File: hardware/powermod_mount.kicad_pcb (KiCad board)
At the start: 4 copper layers, 76 x 46 mm, 76 parts, among them J1 USB_C_IN, J2 USB_C_OUT, J3 JST_PH_2, J4 STEMMA_QT, J5 UPDI_HDR, Q1 AON7407, Q2 AON7407, Q3 BSS138, SW1 BUTTON, U1 BM8563, U2 ATtiny1617, U3 TPS63020DSJR, U4 TP4056, U5 XC6206P332MR, Y1 32.768kHz

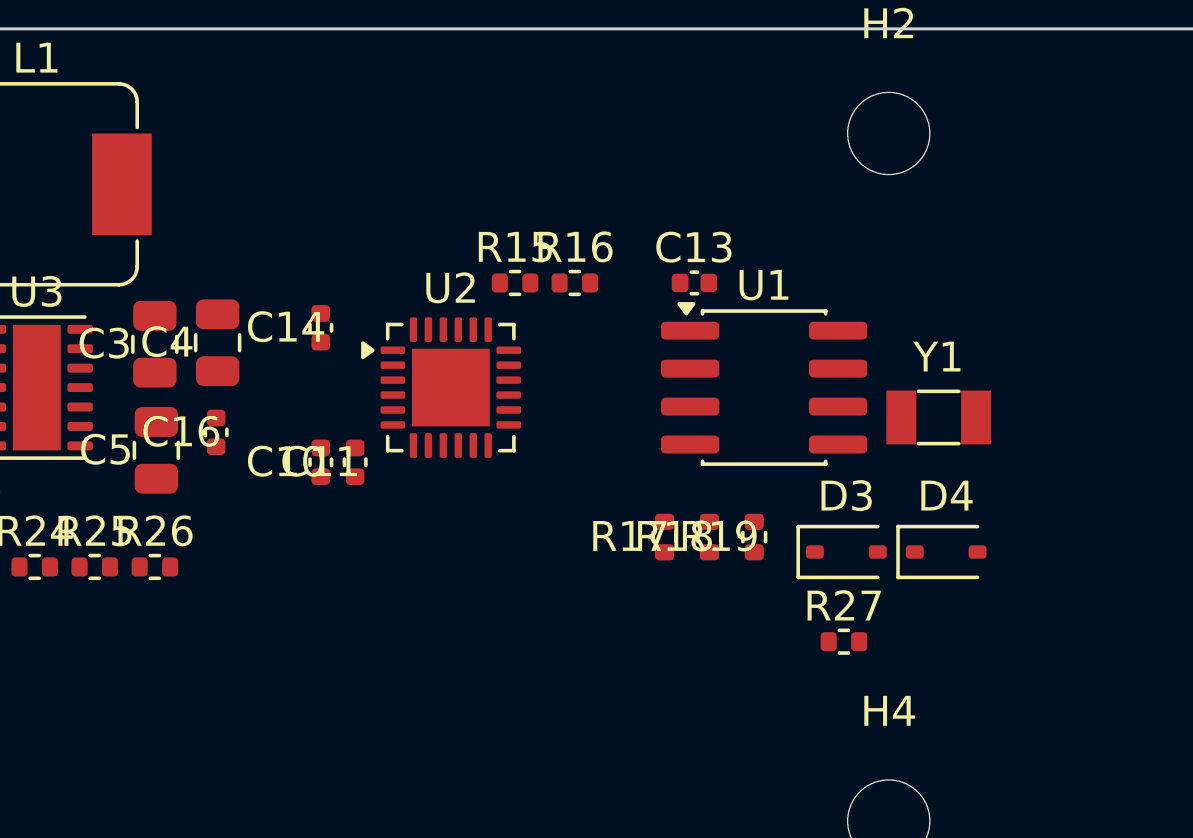
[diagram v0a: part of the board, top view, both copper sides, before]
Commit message: attiny: swap MCU to ATtiny1616 SOIC-20 — breaks the QFN routing wall
The 24-pin QFN (0.5mm pitch) was the persistent autorouting blocker: two of
its pins could never escape, boxed in by their routed neighbours, and no
placement or router technique moved them. Swapping to the ATtiny1616 in
SOIC-20 (1.27mm pitch, 2.5x coarser, no exposed pad, hand-solderable) removes
that wall entirely -- verified: the MCU pins (3V3, Q1_GATE_DRV) that were stuck
across every prior attempt now route, and the residual is ordinary nets
(VBUS/VOUT pour connections, GND stitching), no escape wall.

Electrical: we used exactly 18 signals and the SOIC-20 has exactly 18 I/O, so
it fits -- at the cost of the 4 spare pins the 24-pin had. Four signals moved
off pins the 20-pin package lacks (LED_BAT_A/B off PB6/PB7 -> PA6/PA7, CHG_CE
off PC4 -> PC0, RTC_SCL off PC5 -> PC1); all are plain GPIO and the async-wake
(PC2/PA2), TWI (PB0/PB1), ADC (PA4/PA5) and UPDI (PA0) pins are unchanged.

Pinout taken from KiCad's ATtiny406-S base symbol (the shared 20-pin tinyAVR-1
map), NOT a web summary (which had it wrong). Footprint SOIC-20W_7.5x12.8mm.
LCSC C2891852 to confirm at order time. netlist self-test + ERC both clean
(72 components, 231 pins). On the attiny-soic20 branch.

Co-Authored-By: Claude Opus 4.8 <noreply@anthropic.com>
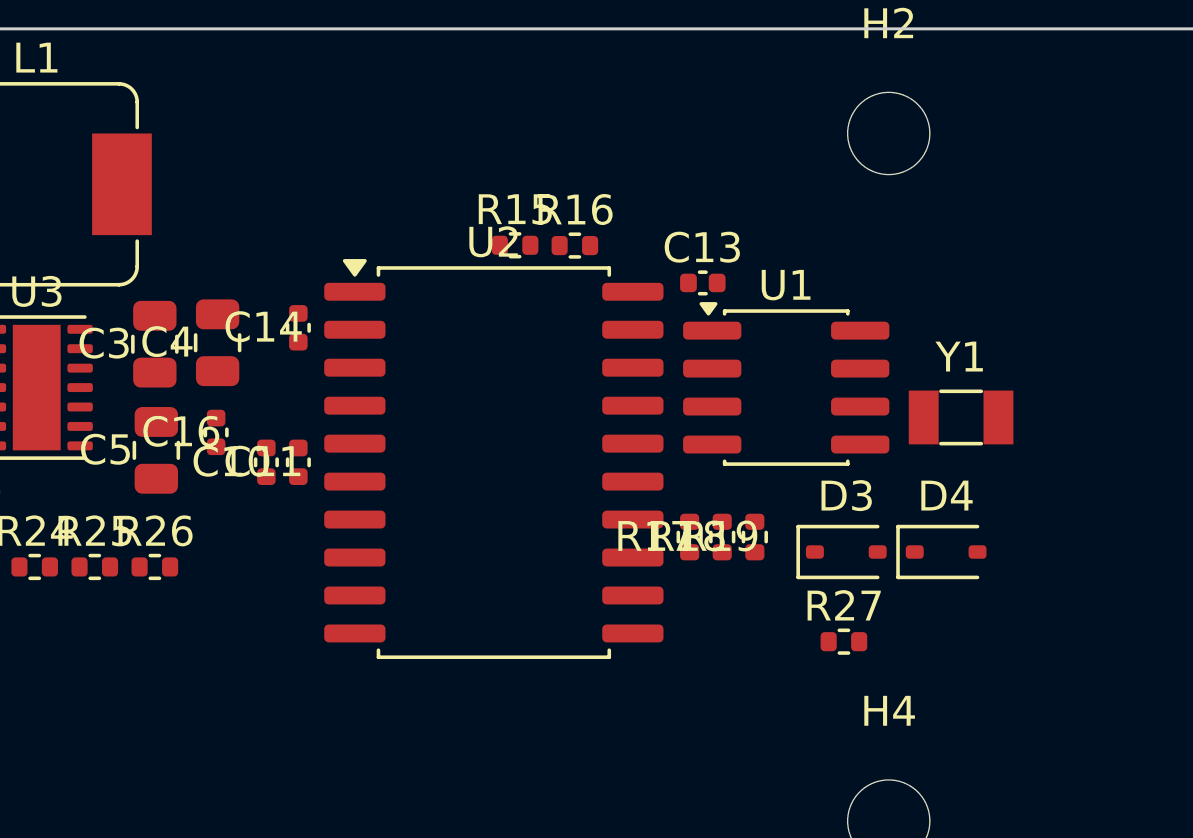
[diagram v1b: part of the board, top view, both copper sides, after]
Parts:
- U2: value ATtiny1617 -> ATtiny1616; footprint QFN-24-1EP_4x4mm_P0.5mm_EP2.6x2.6mm -> SOIC-20W_7.5x12.8mm_P1.27mm
- moved U2 2.89 mm to (48.3, 14.5)
- moved C11 1.90 mm to (41.8, 14.5)
- moved C10 1.82 mm to (40.7, 14.5)
- moved R15 1.26 mm to (49.0, 7.24)
- moved R16 1.25 mm to (51.0, 7.25)
- moved R17 0.84 mm to (54.8, 17.0)
- moved C14 0.75 mm to (41.8, 10.0)
- moved Y1 0.75 mm to (63.9, 13.0)
- moved U1 0.74 mm to (58.1, 12.0)
- moved R18 0.43 mm to (55.9, 17.0)
- moved C13 0.28 mm to (55.3, 8.50)
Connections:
- U2 pad 1: BUTTON -> 3V3
- U2 pad 10: LED_BAT_A -> SDA
- U2 pad 11: CHG_STDBY -> SCL
- U2 pad 12: CHG_CHRG -> CHG_CE
- U2 pad 13: LED_PWR_B -> RTC_SCL
- U2 pad 14: LED_PWR_A -> RTC_INT
- U2 pad 15: SDA -> Q1_GATE_DRV
- U2 pad 16: SCL -> UPDI
- U2 pad 17: (no net) -> RTC_SDA
- U2 pad 18: (no net) -> BUTTON
- U2 pad 19: RTC_INT -> CONV_EN
- U2 pad 2: CONV_EN -> VBAT_DIV
- U2 pad 20: Q1_GATE_DRV -> GND
- U2 pad 3: GND -> VBUS_DIV
- U2 pad 4: 3V3 -> LED_BAT_A
- U2 pad 5: VBAT_DIV -> LED_BAT_B
- U2 pad 6: VBUS_DIV -> CHG_STDBY
- U2 pad 7: (no net) -> CHG_CHRG
- U2 pad 8: (no net) -> LED_PWR_B
- U2 pad 9: LED_BAT_B -> LED_PWR_A

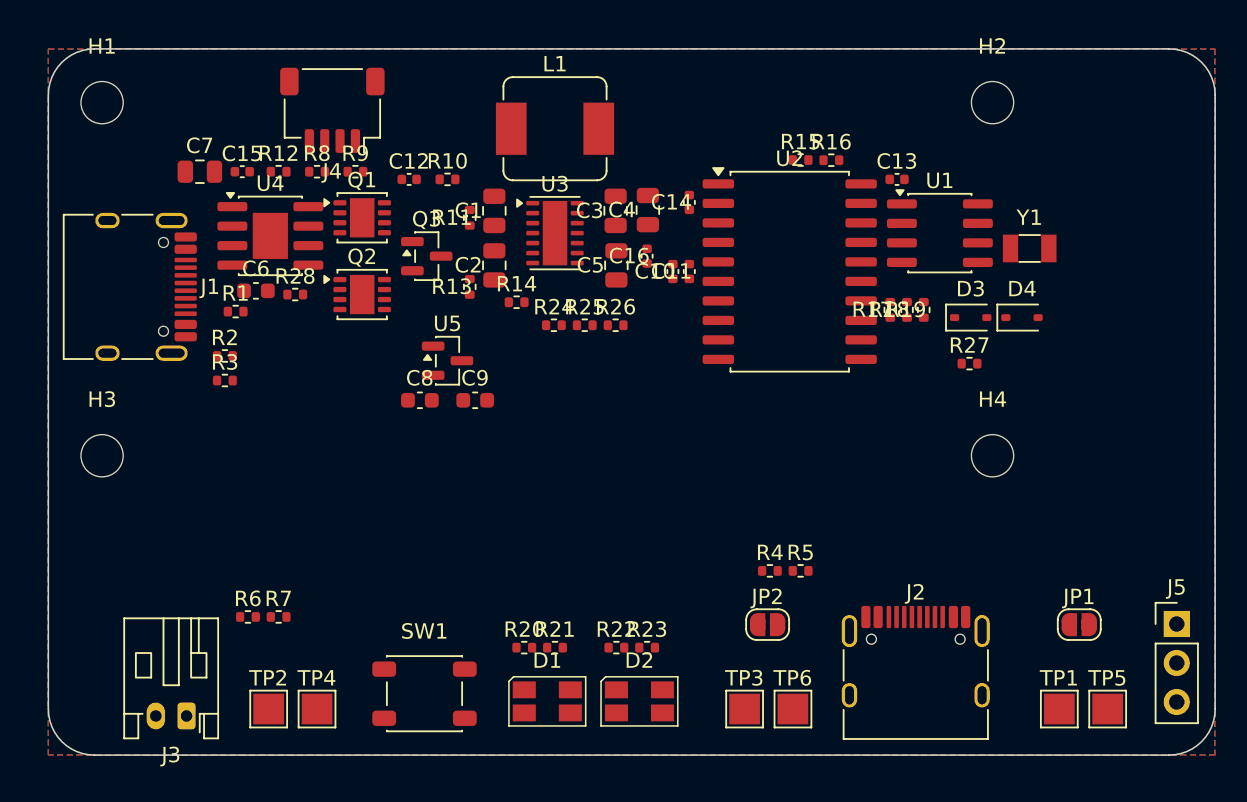
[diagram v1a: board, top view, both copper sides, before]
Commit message: hardware: pre-fab audit + D5 supercap-drain fix; mount board final
Full pre-fab audit (PREFAB_AUDIT.md): board verified pad-for-pad against
netlist.py (214/214 + 11 NC), every IC pinout re-checked against datasheets,
all operating points computed (FB divider exactly 5.000/3.278V via JP2, ADC
ranges, gate drive, ~7.5uA off-state drain). Findings fixed:

- D5 (1N4148WS) added in the VBACKUP charge path (3V3 -> R27 -> D5 -> JP1,
  new net CHG_JPD): without it the supercap back-drains through R27 into the
  dead 3V3 rail at ~3mA exactly when backup is needed.
- 2 PGND vias added in U3's exposed pad (the TPS63020 4A power-ground return
  had no via to the In1 plane within 3.5mm).
- USB-C merged-pad footprint lib (powermod.pretty) now tracked; J1/J2 use it.
- finish_board.py: reusable SES-import + GND-stitch + island-tie + refill
  finisher. place_constrained.py: constraint-aware force-directed placer.

Board state: 0 unconnected, 0 clearance; only the 4 intrinsic track_width
necks at U3's 0.65mm pins remain. Placement + USB-C escapes are hand-routed
(never regenerate the board from netlist.py).

Co-Authored-By: Claude Opus 4.8 <noreply@anthropic.com>
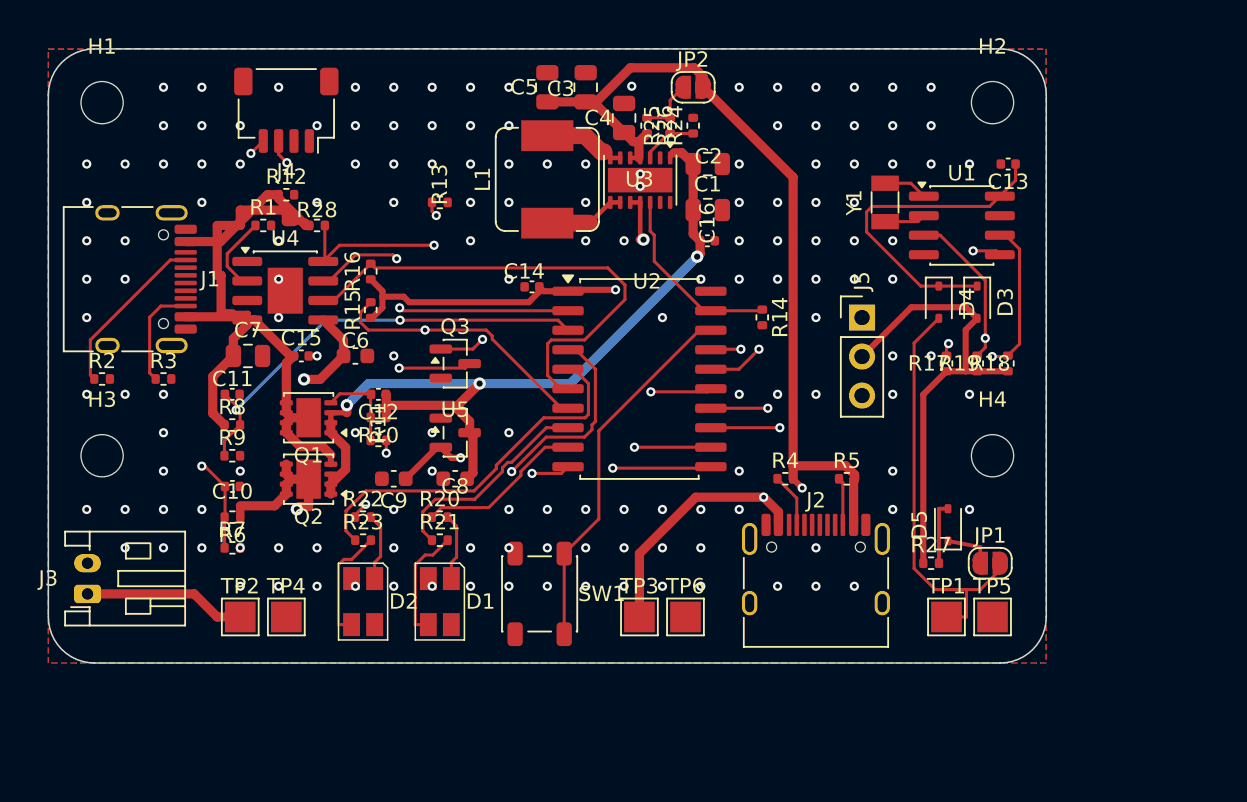
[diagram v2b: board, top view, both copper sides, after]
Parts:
- added D5: 1N4148WS, D_SOD-323, F.Cu at (58.6, 31.0)
- J1, J2: footprint USB_C_Receptacle_HRO_TYPE-C-31-M-12 -> USB_C_Receptacle_TYPE-C_16P_PowerMerged
- moved JP2 35.3 mm to (42.0, 2.50)
- moved C10 31.9 mm to (12.0, 28.5), turned to 0 degrees
- moved R16 30.9 mm to (21.0, 14.5), turned to 90 degrees
- moved C11 30.8 mm to (12.0, 22.5), turned to 0 degrees
- moved R15 29.7 mm to (21.0, 17.0), turned to 90 degrees
- moved J5 28.6 mm to (53.0, 17.5)
- moved R9 20.2 mm to (12.0, 26.5)
- moved R23 19.8 mm to (20.5, 32.0)
- moved D2 19.1 mm to (20.5, 36.0), turned to -90 degrees
- moved R22 18.6 mm to (20.5, 30.5)
- moved R8 17.4 mm to (12.0, 24.5)
- moved R10 16.1 mm to (21.5, 24.0), turned to 180 degrees
- moved R14 16.0 mm to (46.5, 17.5), turned to -90 degrees
- moved R24 15.9 mm to (42.0, 5.00), turned to 90 degrees
- moved R11 15.7 mm to (21.5, 25.5), turned to 0 degrees
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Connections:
- J1 pad SH: (no net) -> GND
- J2 pad SH: (no net) -> GND
- JP1 pad 1: CHG_JP -> CHG_JPD
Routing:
- net 3V3: track 0.00 -> 93.0 mm, vias 0 -> 2
- net VOUT: track 0.00 -> 73.3 mm, vias 0 -> 2
- net VSYS: track 0.00 -> 64.2 mm, vias 0 -> 4
- net VBUS: track 0.00 -> 53.3 mm
- net VBAT_DIV: track 0.00 -> 53.2 mm, vias 0 -> 2
- net VBAT: track 0.00 -> 51.3 mm, vias 0 -> 2
- net SCL: track 0.00 -> 40.8 mm, vias 0 -> 2
- net Q1_GATE_DRV: track 0.00 -> 36.6 mm, vias 0 -> 3
- net CHG_CE: track 0.00 -> 33.6 mm, vias 0 -> 2
- net CHG_STDBY: track 0.00 -> 32.2 mm
- net SDA: track 0.00 -> 31.0 mm, vias 0 -> 2
- net RTC_INT: track 0.00 -> 30.4 mm, vias 0 -> 2
- net RTC_SCL: track 0.00 -> 30.2 mm, vias 0 -> 2
- net VBUS_DIV: track 0.00 -> 29.2 mm, vias 0 -> 2
- net CHG_CHRG: track 0.00 -> 28.5 mm, vias 0 -> 2
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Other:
- board size 76 x 46 mm -> 65 x 40 mm
